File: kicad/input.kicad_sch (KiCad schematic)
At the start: 217 parts, among them J1 IN_1, J2 IN_2, Q1 CSD13380F3, Q5 CSD13380F3, SW1 RotaryEncoder, SW10 DG1411EEQ, SW11 DG1413EEQ, SW17 SW_Push, SW18 SW_Push, SW3 DG1413EEQ, SW4 DG1411EEQ, SW5 DG1413EEQ, SW6 DG1413EEQ, SW7 RotaryEncoder, SW9 DG1413EEQ, U1 THAT5263, U10 THAT1206, U2 THAT1580, U24 OPA1612AxD, U3 OPA1637, U4 THAT1206, U5 OPA1612AxD, U6 OPA1642, U7 THAT1580, U8 TXE8116-Q1, U9 OPA1637

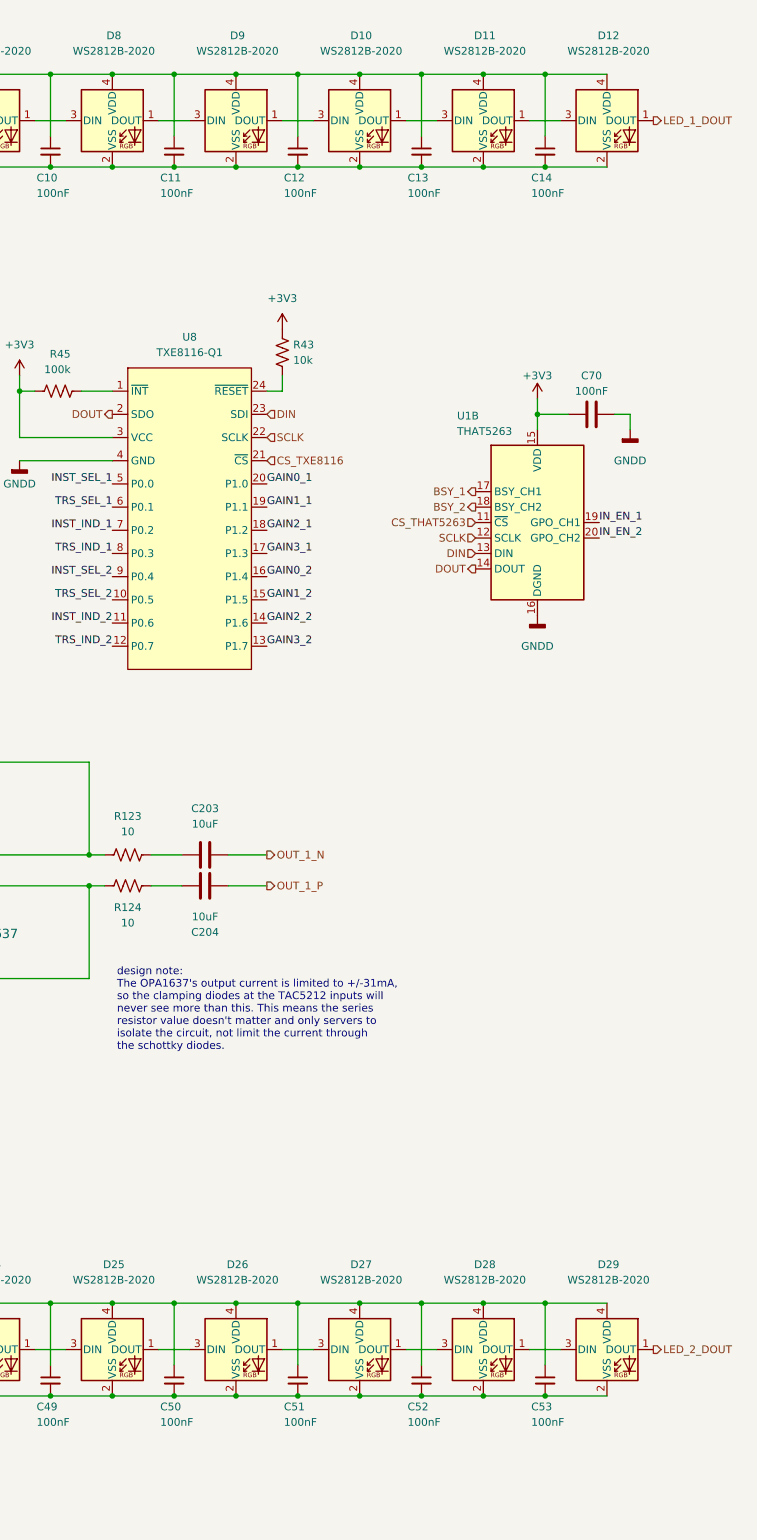
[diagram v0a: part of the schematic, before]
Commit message: reduced ws2812 count
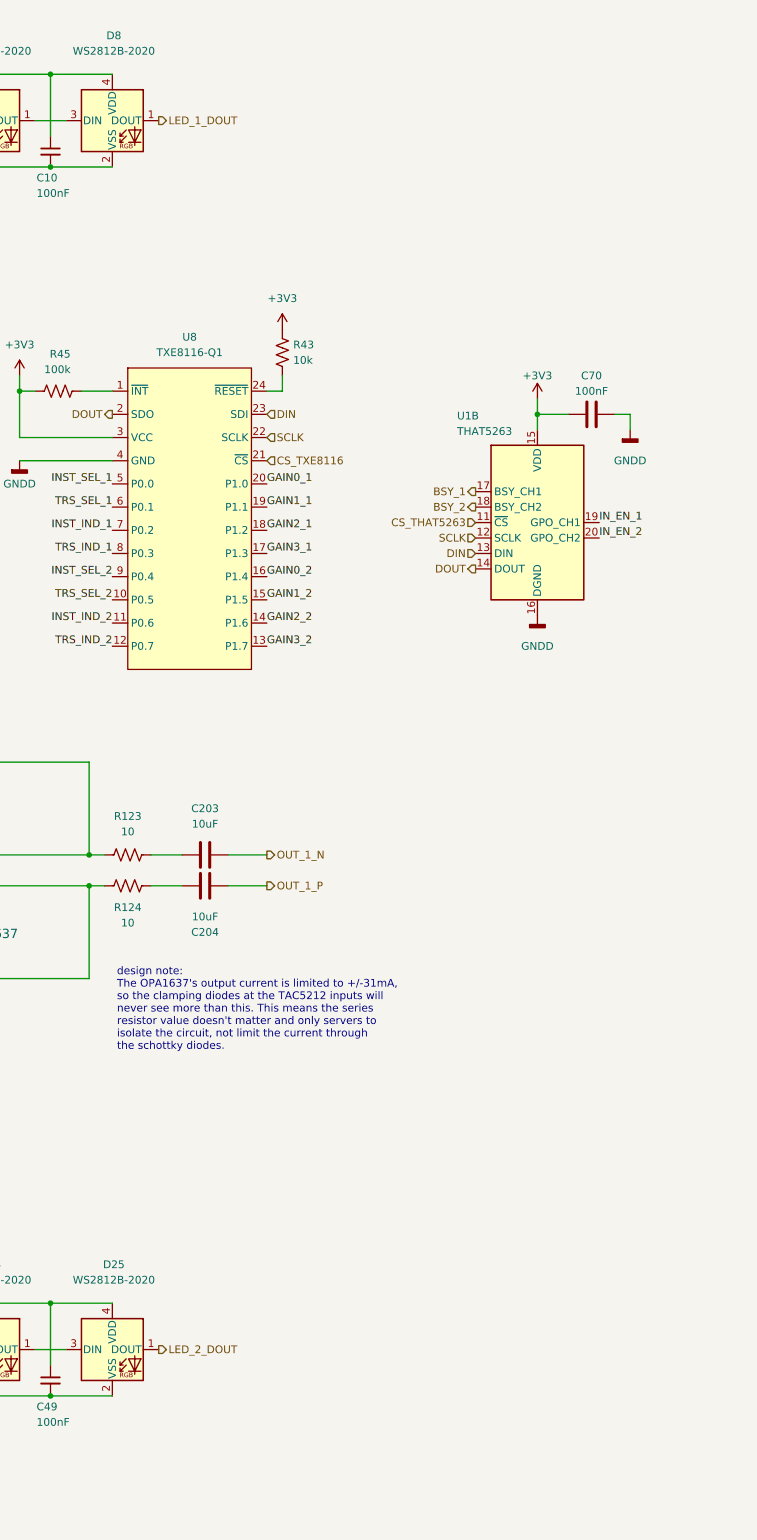
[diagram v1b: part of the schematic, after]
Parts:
- removed C11, C12, C13, C14, C50, C51, C52, C53: 100nF, symbol Device:C_Small
- removed D10, D11, D12, D26, D27, D28, D29, D9: WS2812B-2020, LED_SMD:LED_WS2812B-2020_PLCC4_2.0x2.0mm, symbol LED:WS2812B-2020
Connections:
- net LED_1_DOUT: now also D8.1 (DOUT)
- net LED_2_DOUT: now also D25.1 (DOUT)

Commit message: added footprints
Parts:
- SW1, SW7: footprint (none) -> openmic:PEC11L
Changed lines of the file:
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@@
 			)
 		)
-		(property "Footprint" ""
+		(property "Footprint" "openmic:PEC11L"
 			(at 48.006 49.53 0)
 			(hide yes)
@@
 			)
 		)
-		(property "Footprint" ""
+		(property "Footprint" "openmic:PEC11L"
 			(at 48.006 240.03 0)
 			(hide yes)

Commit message: footprint selection
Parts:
- removed C15, C57: 1000uF, symbol Device:C
- removed C201, C202, C203, C204: 10uF, symbol Device:C
- removed C41: 100uF, symbol Device:C_Polarized_US
- added C11: 100uF, Capacitor_SMD:CP_Elec_6.3x5.4, symbol Device:C_Polarized_US
- added C14, C15: 1000uF, Capacitor_SMD:CP_Elec_8x10.5, symbol Device:C_Polarized_US
- added C50, C51, C52, C53: 10uF, Capacitor_SMD:CP_Elec_6.3x5.4, symbol Device:C_Polarized_US
- C1, C10, C122, C16, C17, C181, C182, C183, C184, C185, C186, C187, C188, C19, C199, C20, C200, C21, C23, C24, C25, C26, C29, C3, C30, C31, C34, C35, C36, C37, C38, C39, C4, C40, C42, C43, C44, C45, C46, C47, C48, C49, C5, C54, C55, C56, C58, C59, C6, C61, C62, C63, C64, C67, C68, C69, C7, C70, C73, C74, C75, C76, C77, C78, C79, C8, C9: footprint (none) -> Capacitor_SMD:C_0603_1608Metric_Pad1.08x0.95mm_HandSolder
- C2, C22, C28, C32, C60, C66, C71: footprint (none) -> Capacitor_SMD:CP_Elec_6.3x5.4
- D13, D30: footprint (none) -> LED_SMD:LED_0603_1608Metric_Pad1.05x0.95mm_HandSolder
- R1, R10, R11, R123, R124, R125, R126, R127, R128, R129, R13, R130, R14, R15, R16, R17, R18, R19, R2, R20, R21, R22, R23, R24, R25, R26, R27, R28, R29, R30, R31, R33, R34, R35, R36, R37, R38, R39, R4, R40, R41, R42, R43, R44, R45, R46, R47, R48, R49, R5, R50, R51, R52, R53, R54, R55, R56, R57, R59, R6, R60, R7, R8, R9: footprint (none) -> Resistor_SMD:R_0603_1608Metric_Pad0.98x0.95mm_HandSolder
- U3, U9: footprint DGK0008A_N -> (none)
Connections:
- net +5V: now also C11.1
- net GNDD: now also C11.2
- net OUT_1_N: now also C50.1
- net OUT_1_P: now also C51.1
- net OUT_2_N: now also C52.1
- net OUT_2_P: now also C53.1
- net at R124.2: now also C51.2
- net at R5.2, U1.7 (RG1_CH1): now also C15.2
- net at U1.6 (RA_CH1), U2.6 (Rg1): now also C15.1
- net at R36.2, U1.23 (RG1_CH2): now also C14.2
- net at U1.22 (RA_CH2), U7.6 (Rg1): now also C14.1
- net at R125.2: now also C52.2
- net at R123.2: now also C50.2
- net at R126.2: now also C53.2

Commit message: footprints
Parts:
- removed J1: IN_1, symbol Connector_Audio:XLR3_AudioJack3_Combo_Ground_Switch
- removed J2: IN_2, symbol Connector_Audio:XLR3_AudioJack3_Combo_Ground_Switch
- added C57, C65: 100nF, Capacitor_SMD:C_0603_1608Metric_Pad1.08x0.95mm_HandSolder, symbol Device:C
- added J3, J4: NCJ10FI-H-0, Connector_Audio:Jack_XLR-6.35mm_Neutrik_NCJ10FI-H-0_Horizontal, symbol Connector_Audio:NCJ10FI-H-0
- added R32, R58: 47k, Resistor_SMD:R_0603_1608Metric_Pad0.98x0.95mm_HandSolder, symbol Device:R_US
- SW10, SW11, SW3, SW4, SW5, SW6, SW9: footprint (none) -> Package_SO:TSSOP-16_4.4x5mm_P0.65mm
- U10, U24, U4, U5: footprint (none) -> Package_SO:SOIC-8_3.9x4.9mm_P1.27mm
- U3, U6, U9: footprint (none) -> Package_SO:VSSOP-8_3x3mm_P0.65mm
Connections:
- net +3V3: now also R32.1, R58.1
- net GNDA: now also C57.2, C65.2, J3.1, J3.G, J3.RN, J3.S, J3.TN, J4.1, J4.G, J4.RN, J4.S, J4.TN
- net TRS_IND_1: now also J3.SN
- net TRS_IND_2: now also J4.SN
- net at C60.1, C61.1, C63.1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: now also J4.2
- net at C63.2, C66.1, C67.1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: now also J4.3
- net at C75.1, R41.1: now also J4.T
- net at C76.1, SW9.14 (S2), SW9.3 (S1): now also J4.R
- net at C25.2, C28.1, C29.1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: now also J3.3
- net at C22.1, C23.1, C25.1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: now also J3.2
- net at C37.1, SW3.14 (S2), SW3.3 (S1): now also J3.R
- net at C36.1, R27.1: now also J3.T
- new net XLR_IND_1: C57.1, C65.1, J3.GN, J4.GN, R32.2, R58.2

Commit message: footprints
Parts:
- U8: footprint (none) -> openmic:VSSOP-24
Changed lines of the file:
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@@
 			)
 		)
-		(property "Footprint" ""
+		(property "Footprint" "openmic:VSSOP-24"
 			(at 448.31 101.6 0)
 			(hide yes)

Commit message: xlr ind (#16)
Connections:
- net XLR_IND_1: no longer C65.1, J4.GN, R58.2
- new net XLR_IND_2: C65.1, J4.GN, R58.2
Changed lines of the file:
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@@
 		)
 	)
-	(hierarchical_label "XLR_IND_1"
+	(hierarchical_label "XLR_IND_2"
 		(shape output)
 		(at 29.21 294.64 180)

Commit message: INA1650 (#10)
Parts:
- removed C32, C71: 220uF, Capacitor_SMD:CP_Elec_6.3x5.4, symbol Device:C_Polarized_US
- removed C34, C39, C73, C78: 100nF, Capacitor_SMD:C_0603_1608Metric_Pad1.08x0.95mm_HandSolder, symbol Device:C
- removed C35, C38, C74, C77: 470pF, Capacitor_SMD:C_0603_1608Metric_Pad1.08x0.95mm_HandSolder, symbol Device:C
- removed C40, C79: 100pF, Capacitor_SMD:C_0603_1608Metric_Pad1.08x0.95mm_HandSolder, symbol Device:C
- removed R22, R27, R53: 100, Resistor_SMD:R_0603_1608Metric_Pad0.98x0.95mm_HandSolder, symbol Device:R_US
- removed R46: 4k7, Resistor_SMD:R_0603_1608Metric_Pad0.98x0.95mm_HandSolder, symbol Device:R_US
- removed U10, U4: THAT1206, Package_SO:SOIC-8_3.9x4.9mm_P1.27mm, symbol openmic:THAT120x
- added C100, C104, C106, C115: 10uF, Capacitor_SMD:C_0603_1608Metric_Pad1.08x0.95mm_HandSolder, symbol Device:C
- added C72, C87: 100nF, Capacitor_SMD:C_0603_1608Metric_Pad1.08x0.95mm_HandSolder, symbol Device:C
- added C98, C99: 1uF, Capacitor_SMD:C_0603_1608Metric_Pad1.08x0.95mm_HandSolder, symbol Device:C
- added R12: 1M, Resistor_SMD:R_0603_1608Metric_Pad0.98x0.95mm_HandSolder, symbol Device:R_US
- added R121: 100, Resistor_SMD:R_0603_1608Metric_Pad0.98x0.95mm_HandSolder, symbol Device:R_US
- added R134, R137, R80, R87: 100k, Resistor_SMD:R_0603_1608Metric_Pad0.98x0.95mm_HandSolder, symbol Device:R_US
- added U14: INA1650, Package_SO:TSSOP-14_4.4x5mm_P0.65mm, symbol openmic:INA1650
- R15: value 4k7 -> 1M
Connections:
- net +15V: now also C72.2, C98.2, U14.1 (VCC)
- net -15V: now also C87.1, C99.2, U14.14 (VEE)
- net GNDA: now also R15.1, C72.1, C87.2, C98.1, C99.1, R12.1, R134.2, R137.2, R80.2, R87.2, U14.12 (REF), U14.9 (REF)
- net at D68.3 (K): now also SW9.15 (D2), C106.2, R137.1
- net at SW9.10 (D3): now also C115.2, R134.1
- net at SW6.11 (S3): now also U14.8 (OUT)
- net at D66.3 (K): now also SW3.15 (D2), C100.2, R87.1
- net at U6.3 (+): now also R121.2; no longer SW3.7 (D4)
- net at C75.1, J4.T: now also D67.3 (K), SW9.11 (S3), SW9.6 (S4); no longer R41.1
- net at SW3.10 (D3): now also C104.2, R80.1
- net at D65.3 (K), SW3.11 (S3), SW3.6 (S4): now also C36.1, J3.T
- net at R15.2: now also U14.6 (COM)
- net at U6.5 (+): now also R41.2; no longer SW9.7 (D4)
- net at SW6.14 (S2): now also U14.13 (OUT)
- new net: C115.1, U14.5 (IN-)
- new net: C106.1, U14.7 (IN+)
- new net: C100.1, U14.2 (IN+)
- new net: R12.2, U14.3 (COM)
- new net: C104.1, U14.4 (IN-)
- new net: R41.1, SW9.7 (D4)
- new net: R121.1, SW3.7 (D4)
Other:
- moved on the sheet: C181, C182, D65, D66, D67, D68, SW3C, SW3D, SW3E, SW6B, SW9C, SW9D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

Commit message: output schematic pdfs
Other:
- note removed: "mic/line/inst in"
- company: (none) -> OpenMic
- title: (none) -> Audio inputs
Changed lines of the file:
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@@
 	(generator_version "10.0")
 	(paper "C")
+	(title_block
+		(title "Audio inputs")
+		(date "2026-05-15")
+		(company "OpenMic")
+	)
 	(text "design note:\nThe OPA1637's output current is limited to +/-31mA,\nso the clamping diodes at the TAC5212 inputs will\nnever see more than this. This means the series \nresistor value doesn't matter and only servers to\nisolate the circuit, not limit the current through \nthe schottky diodes."
 		(exclude_from_sim no)
@@
 		)
 	)
-	(text "mic/line/inst in"
-		(exclude_from_sim no)
-		(at 472.948 398.272 0)
-		(effects
-			(font
-				(size 2.54 2.54)
-			)
-			(justify left bottom)
-		)
-	)
